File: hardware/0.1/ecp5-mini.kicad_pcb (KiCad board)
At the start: 4 copper layers, 52 x 27 mm, 102 parts, among them J1 Micro_SD_Card, J2 JTAG, J3 S7 Mini, J4 S7 Mini, J5 USB_C_Receptacle_USB2.0, Q1 BSS138, Q2 BSS138, Q3 BSS138, Q4 BSS138, SW1 SW_Push, U1 ECP5U_12_CABGA256, U2 TLV73325PDBV, U3 TLV62568DBV, U4 USBLC6-2SC6, U5 TLV62568DBV, U6 W25Q128JVSIQ, U7 S27KL0641, X1 DSC6101CI2A-016

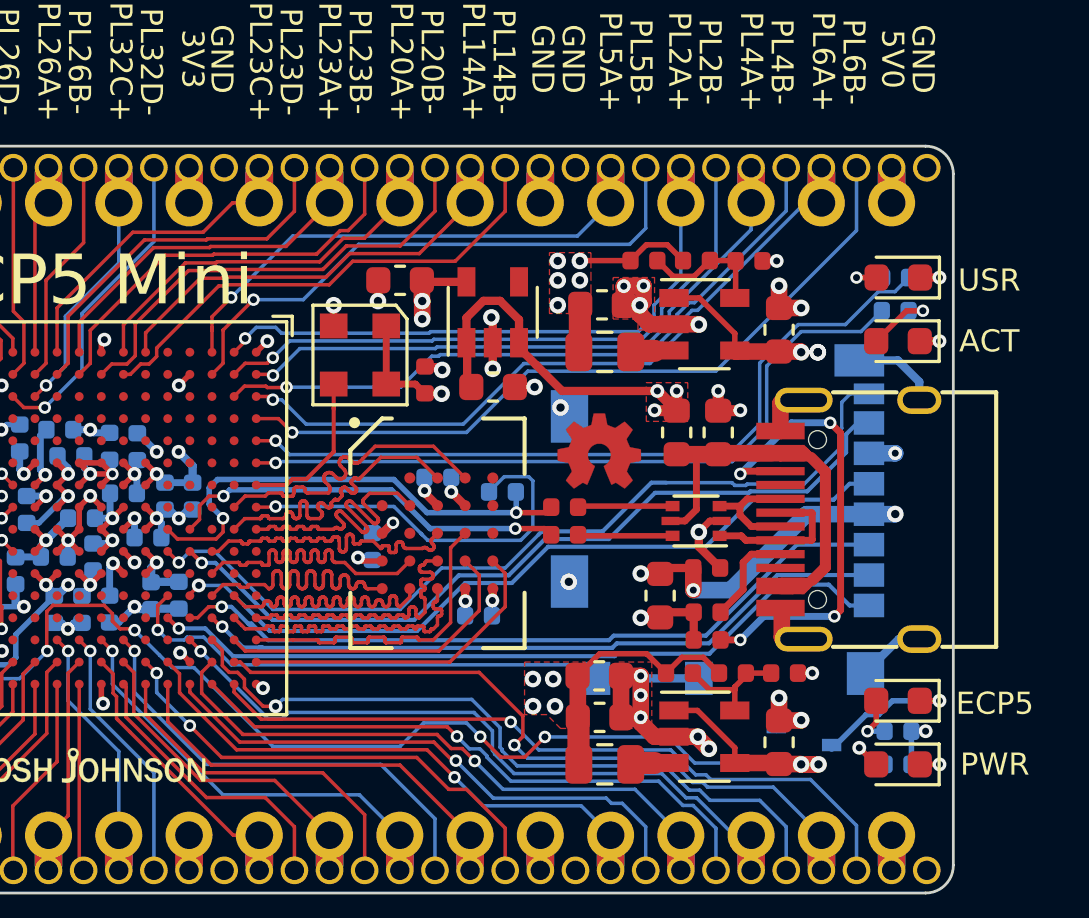
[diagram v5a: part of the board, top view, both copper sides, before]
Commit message: move sd connector
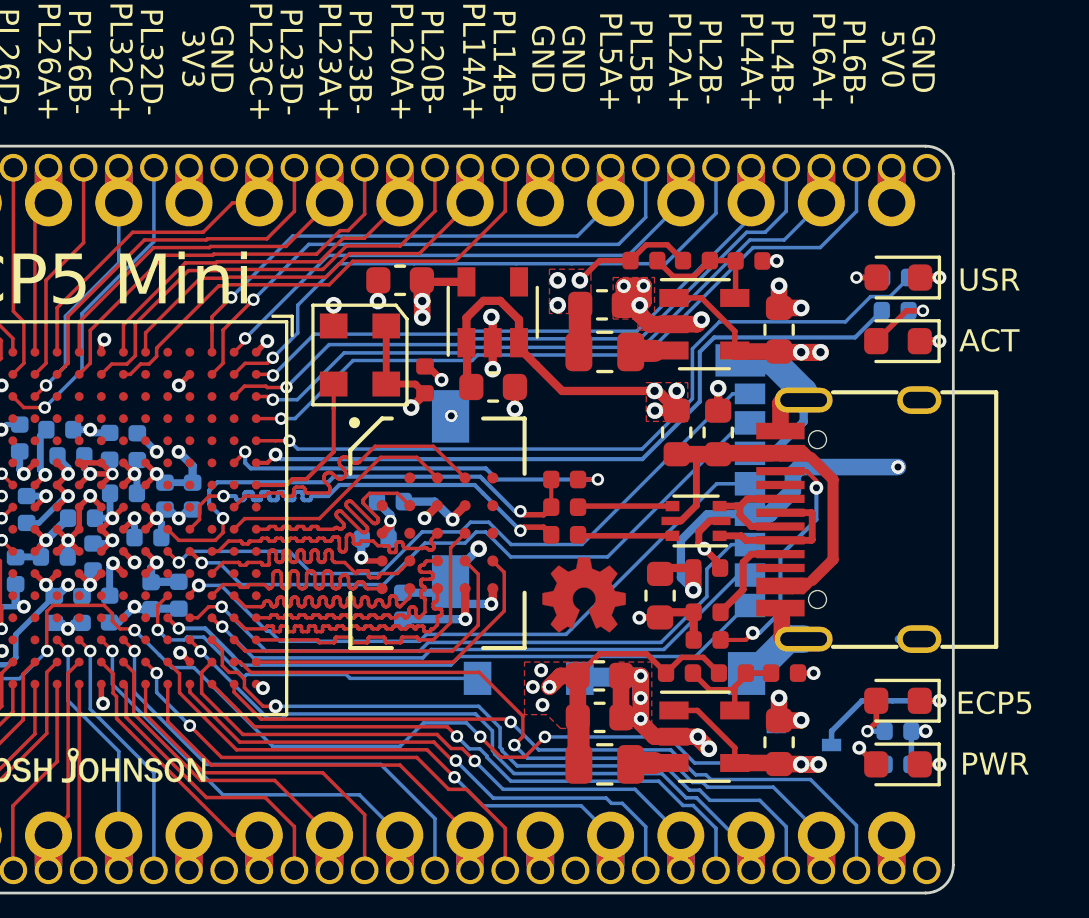
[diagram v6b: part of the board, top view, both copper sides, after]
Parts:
- R11: moved to F.Cu
- moved LOGO2 5.23 mm to (134.8, 97.7)
- moved C45 4.65 mm to (127.3, 95.7)
- moved J1 4.30 mm to (135.4, 95.0)
- moved C47 2.42 mm to (128.3, 98.1)
- moved R11 2.29 mm to (134.2, 93.5), turned to 0 degrees
- moved C46 1.92 mm to (127.8, 94.3)
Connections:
- U1 pad A8: /USB_PU -> Net-(U1-PadA8)
- U1 pad B6: Net-(U1-PadB6) -> /USB_PU
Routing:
- net GND: track 110.0 -> 122.4 mm, vias 66 -> 64
- net Net-(J5-PadB5): track 17.2 -> 9.31 mm, vias 4 -> 2
- net +3V3: track 59.9 -> 66.4 mm, vias 24 -> 21
- net /SD_DAT1: track 30.8 -> 25.1 mm
- net /SD_DAT0: track 28.9 -> 23.9 mm
- net /SD_DAT2: track 27.3 -> 22.7 mm
- net /SD_DET: track 18.1 -> 13.8 mm
- net /SD_DAT3: track 25.4 -> 21.3 mm
- net /SD_CLK: track 27.6 -> 23.6 mm
- net /SD_CMD: track 26.9 -> 23.3 mm
- net /HR_nCS: track 11.7 -> 8.74 mm
- net /USB_D-: track 14.7 -> 16.9 mm
- net /PORT_E1: track 20.5 -> 18.4 mm
- net +5V: track 72.2 -> 73.7 mm, vias 8 -> 7
- net /PORT_E3: track 24.4 -> 23.4 mm
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
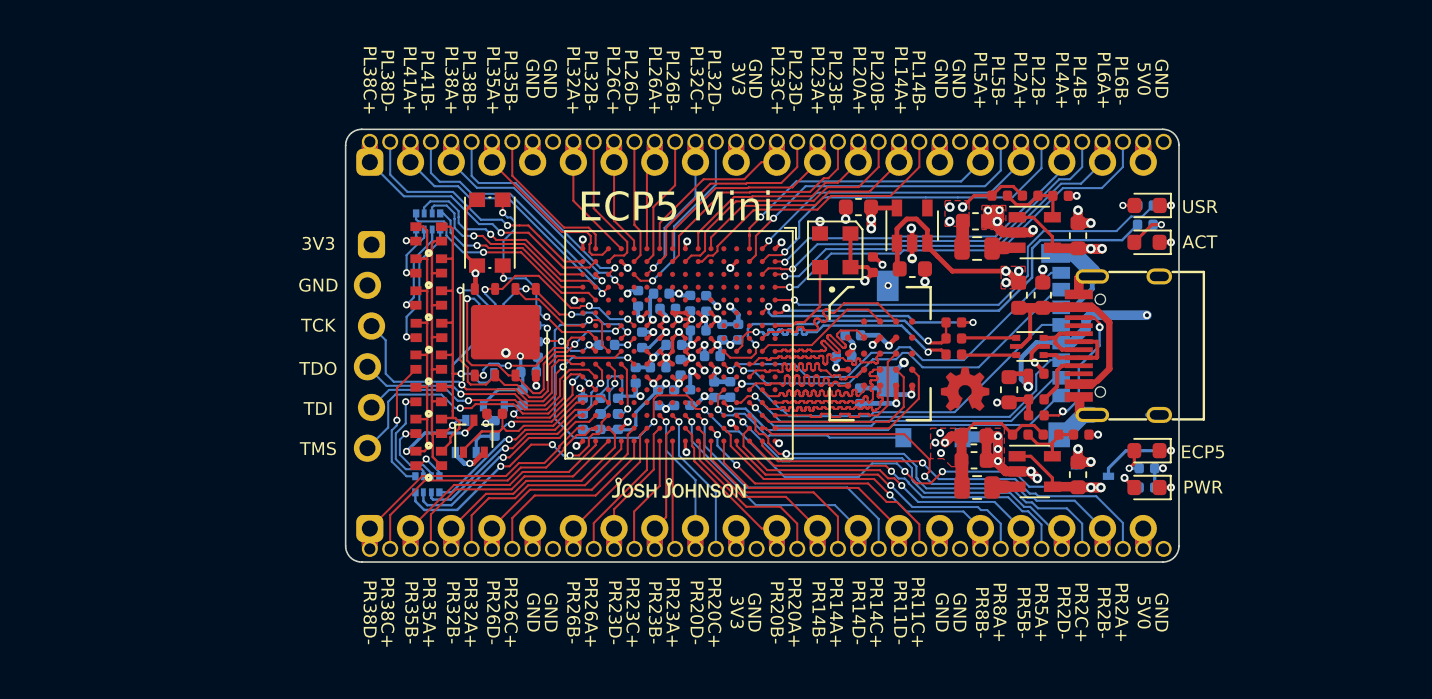
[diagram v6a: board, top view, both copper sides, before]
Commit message: clean up IO routing
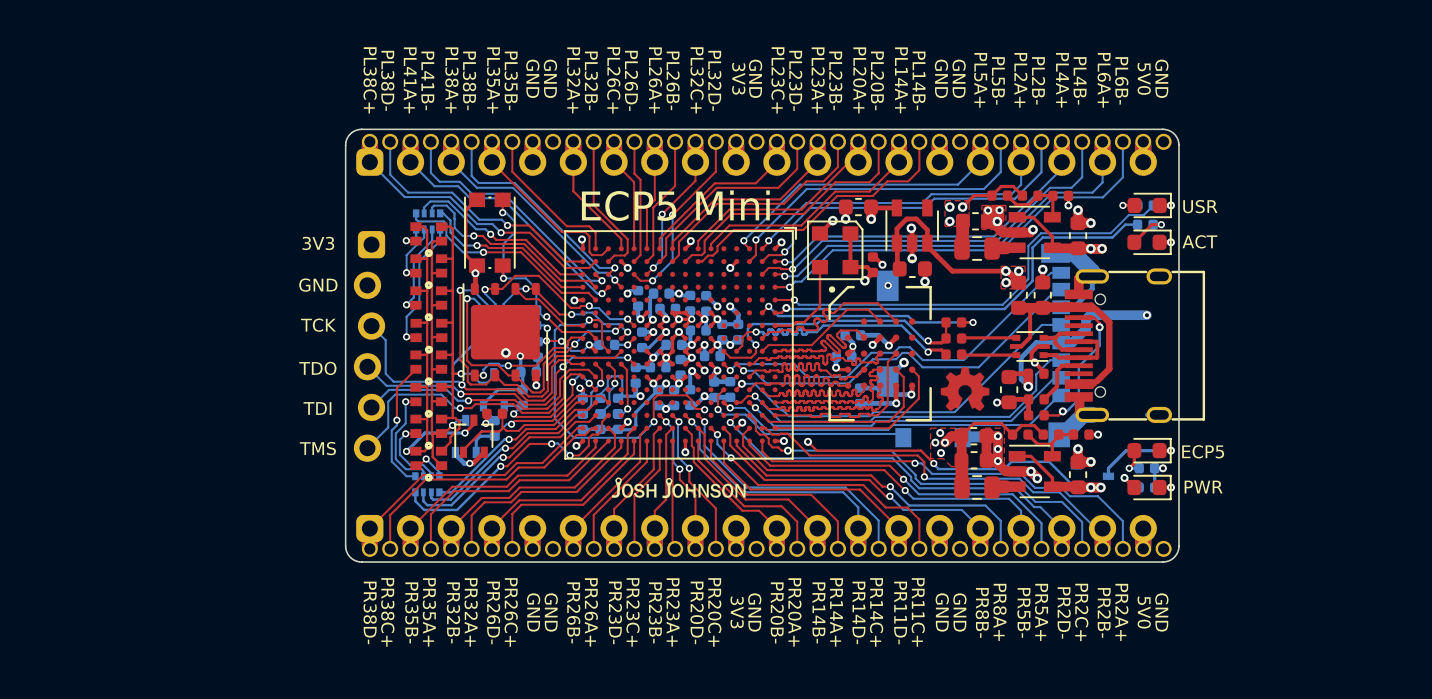
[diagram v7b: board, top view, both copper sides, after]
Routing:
- net /FPGA Config/CFG_CDONE: track 49.7 -> 48.7 mm
- net +2V5: track 30.6 -> 29.8 mm, vias 4 -> 3
- net /PORT_E1: track 18.4 -> 19.3 mm
- net /PORT_C2: track 14.4 -> 15.2 mm
- net /PORT_E3: track 23.4 -> 24.2 mm
- net /PORT_D1: track 20.7 -> 21.4 mm
- net /PORT_F0: track 10.5 -> 9.92 mm
- net /PORT_B7: track 9.45 -> 9.50 mm, vias 1 -> 2
- net /PORT_G7: vias 1 -> 2
- net /PORT_G3: vias 1 -> 2
- net /PORT_B3: vias 1 -> 2

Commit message: update readme
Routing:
- net /PORT_D3: track 24.4 -> 25.2 mm
